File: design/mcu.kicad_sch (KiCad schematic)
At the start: 13 parts, among them U1 STM32F40X_LQFP64, X1 8m

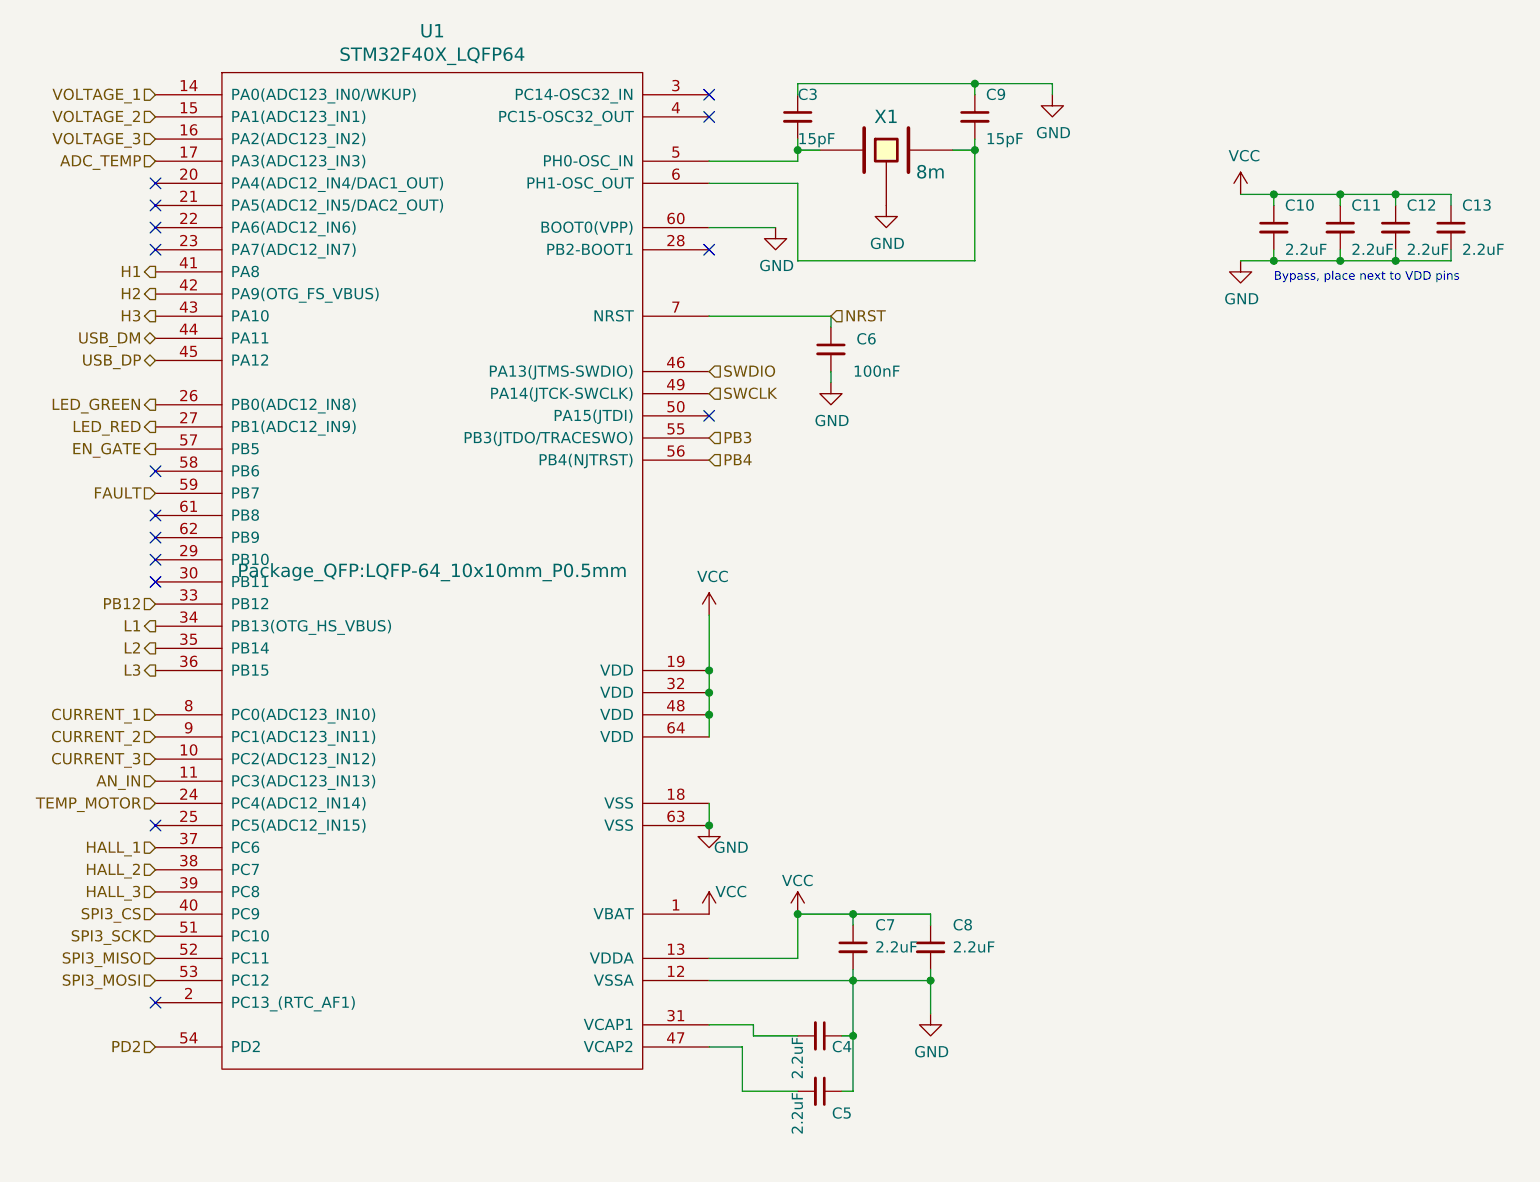
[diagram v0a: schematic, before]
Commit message: Agregado ibom
Pequeños cambios en el esquemático y agregado de ibom
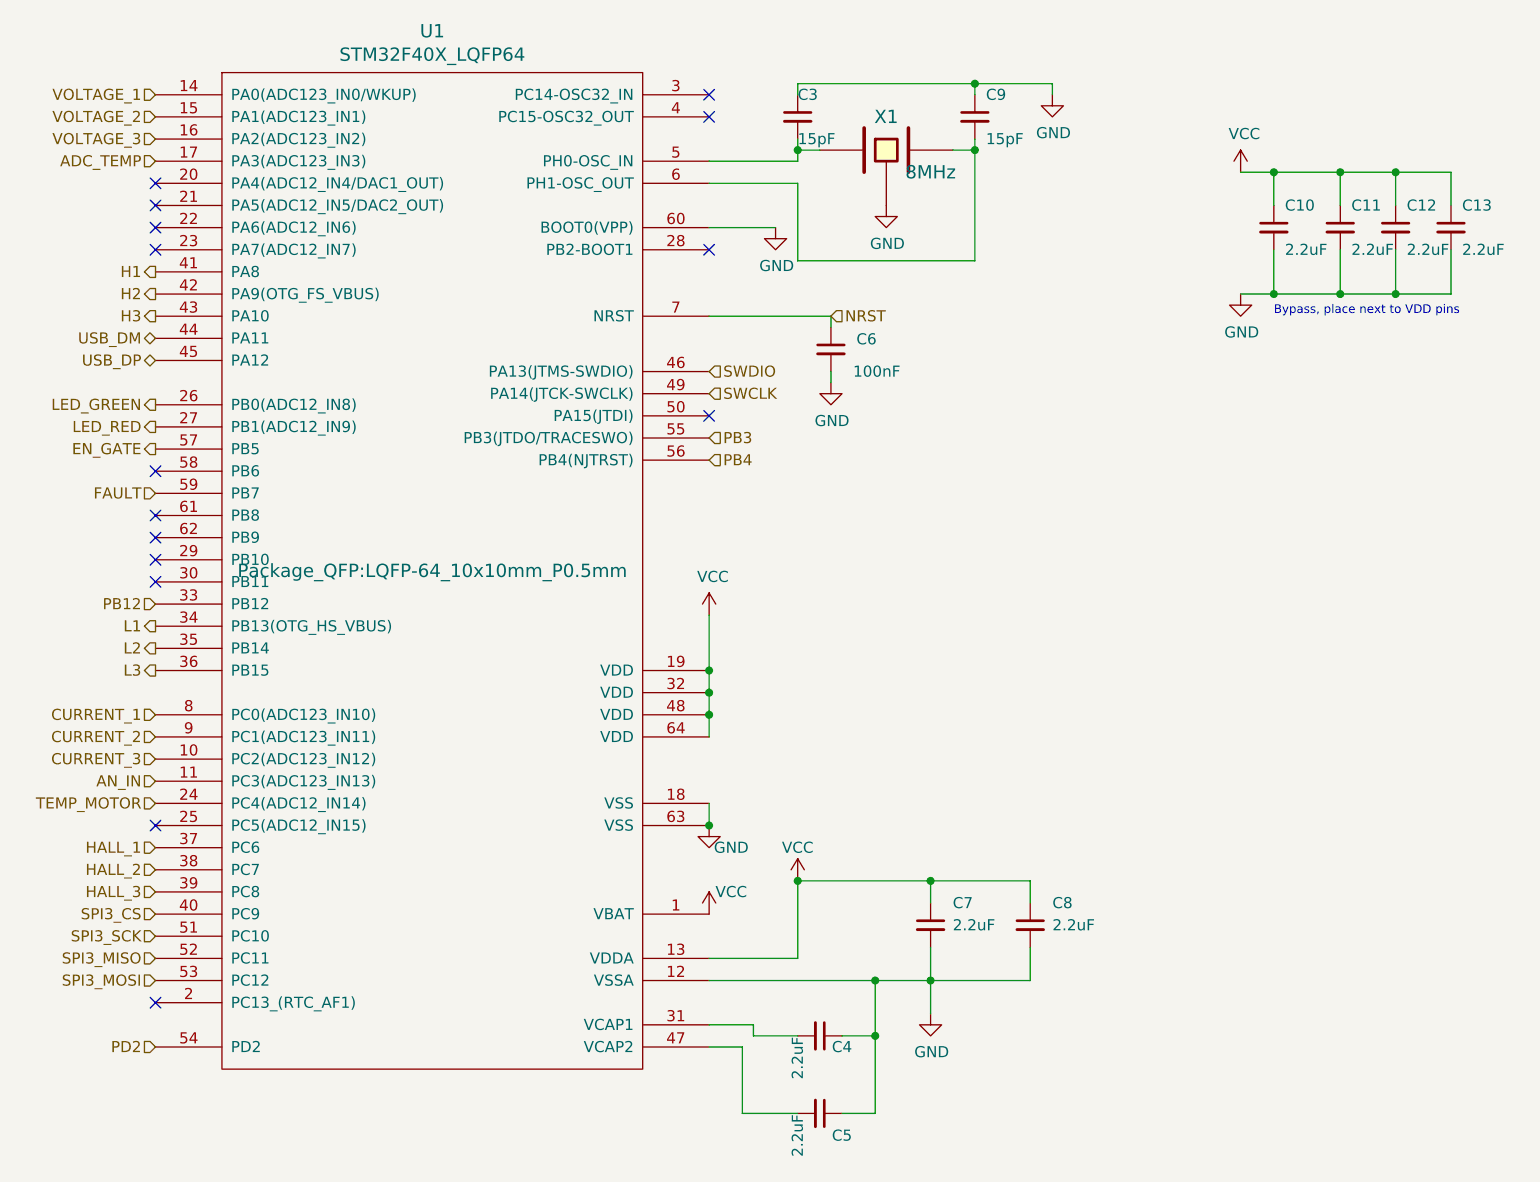
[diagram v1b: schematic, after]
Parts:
- X1: value 8m -> 8MHz
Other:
- moved on the sheet: C5, C7, C8

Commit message: Cambios en el esquemático
- Cambio de Vcc por +3.3V
- Agregado de hoja para desarrollar la entrada de tensión alterna
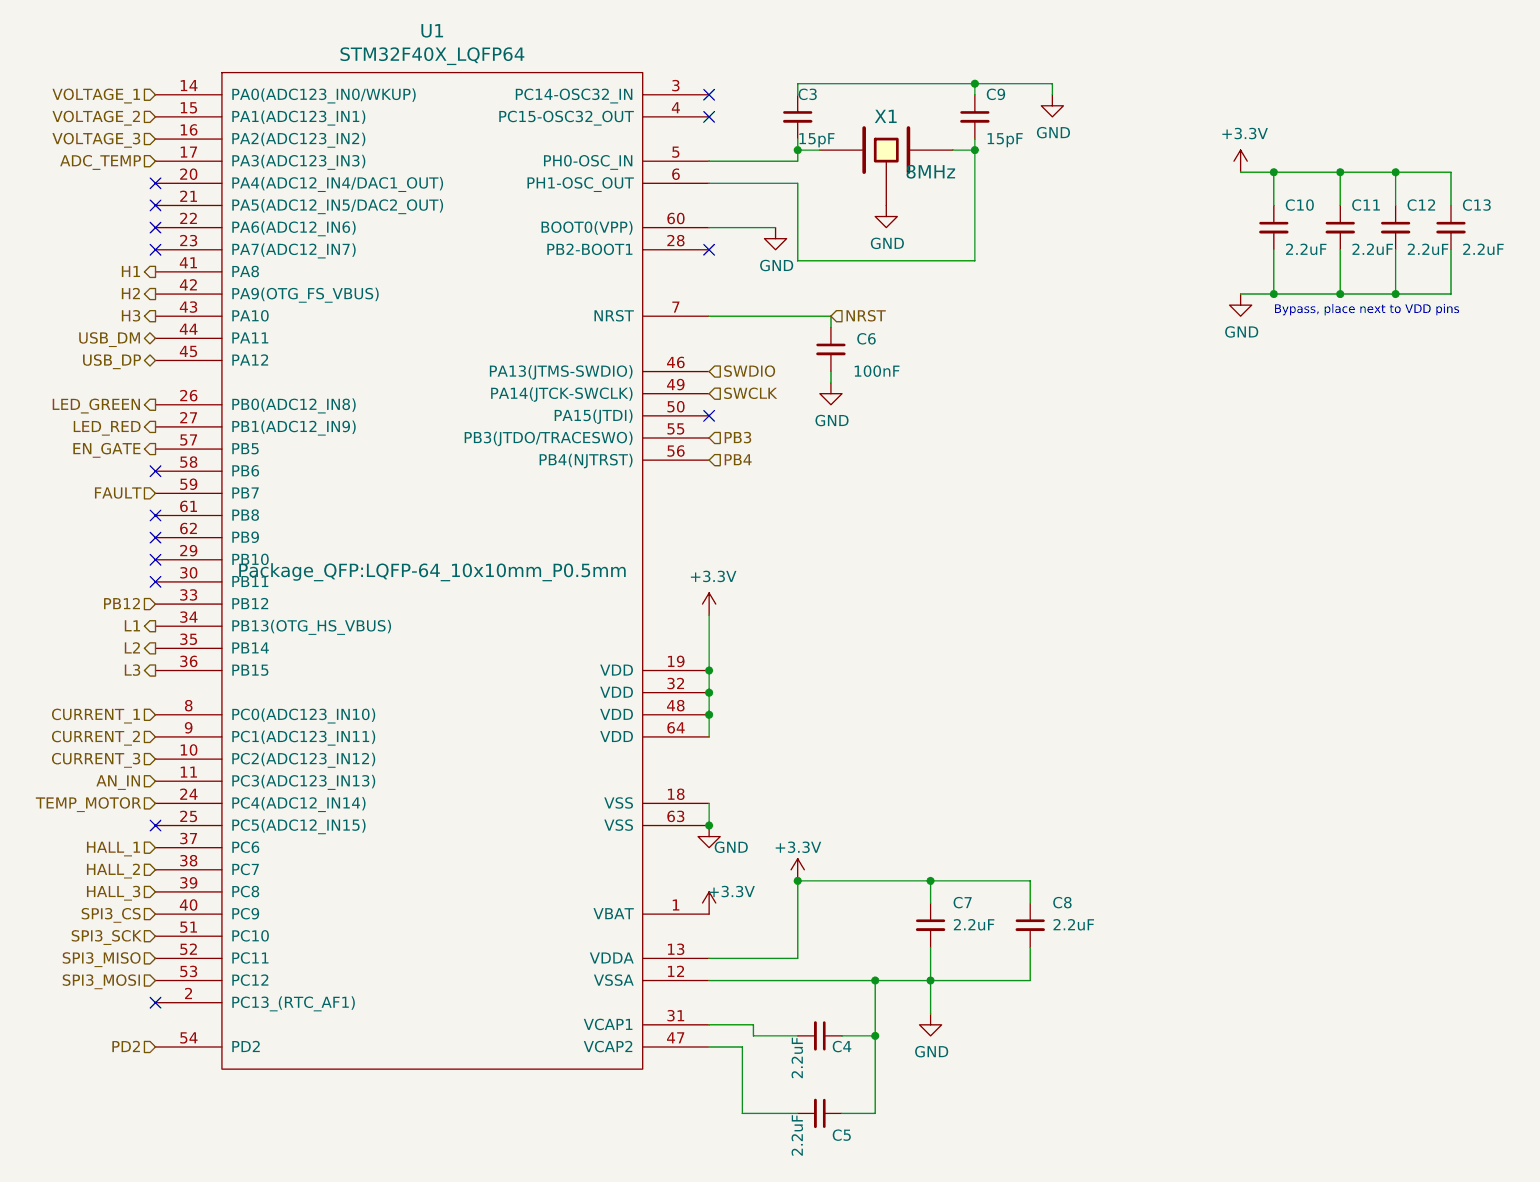
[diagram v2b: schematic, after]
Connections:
- net VCC renamed +3.3V
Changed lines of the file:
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@@
 			)
 		)
-		(property "Value" "VCC"
+		(property "Value" "+3.3V"
 			(at 185.8518 87.0458 0)
 			(effects
@@
 			)
 		)
-		(property "Value" "VCC"
+		(property "Value" "+3.3V"
 			(at 187.96 123.19 0)
 			(effects
@@
 			)
 		)
-		(property "Value" "VCC"
+		(property "Value" "+3.3V"
 			(at 195.58 118.11 0)
 			(effects
@@
 			)
 		)
-		(property "Value" "VCC"
+		(property "Value" "+3.3V"
 			(at 246.8118 36.2458 0)
 			(effects
